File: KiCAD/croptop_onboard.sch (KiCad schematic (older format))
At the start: 64 parts, among them SW1 BTNA, SW2 BTNB, SW3 BTNC, SW4 BTND, U12 Si7006-A20, U13 UCAM-M8Q, U14 W25N01GV, U15 LIS3DH

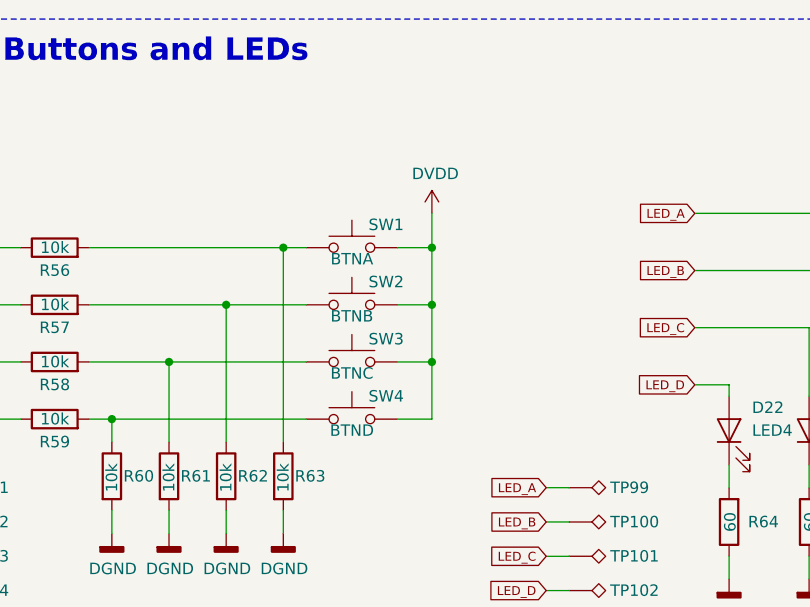
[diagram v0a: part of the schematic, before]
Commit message: Got to PCB layout
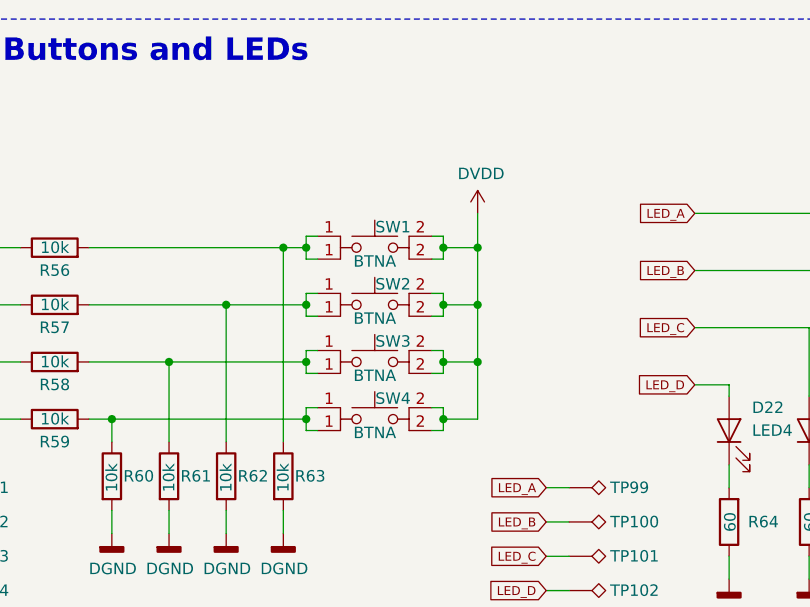
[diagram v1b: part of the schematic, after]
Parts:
- removed SW1: BTNA, symbol Switch:SW_Push
- removed SW2: BTNB, symbol Switch:SW_Push
- removed SW3: BTNC, symbol Switch:SW_Push
- removed SW4: BTND, symbol Switch:SW_Push
- added SW1, SW2, SW3, SW4: BTNA, Button_Switch_SMD:SW_SPST_PTS645, symbol CropTop:SW_Push
- U12: footprint (none) -> croptop:SI7006
- U13: footprint (none) -> croptop:GPS
- U14: footprint (none) -> croptop:W25N01GV
- U15: footprint (none) -> Package_LGA:LGA-16_3x3mm_P0.5mm_LayoutBorder3x5y
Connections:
- net DVDD: now also SW1.2, SW2.2, SW3.2, SW4.2
- net at R59.2, R60.1: now also SW4.1
- net at R58.2, R61.1: now also SW3.1
- net at R57.2, R62.1: now also SW2.1
- net at R56.2, R63.1: now also SW1.1
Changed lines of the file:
@@
 F 0 "U13" H 2500 3125 50  0000 C CNN
 F 1 "UCAM-M8Q" H 2500 3034 50  0000 C CNN
-F 2 "" H 2450 3000 50  0001 C CNN
+F 2 "croptop:GPS" H 2450 3000 50  0001 C CNN
 F 3 "" H 2450 3000 50  0001 C CNN
 	1    2500 2150
@@
 F 0 "U15" H 6900 2950 50  0000 C CNN
 F 1 "LIS3DH" H 7450 2950 50  0000 C CNN
-F 2 "" H 7100 2050 50  0001 C CNN
+F 2 "Package_LGA:LGA-16_3x3mm_P0.5mm_LayoutBorder3x5y" H 7100 2050 50  0001 C CNN
 F 3 "" H 7100 2050 50  0001 C CNN
 	1    7200 2350
@@
 F 0 "U12" H 2050 7275 50  0000 C CNN
 F 1 "Si7006-A20" H 2050 7184 50  0000 C CNN
-F 2 "" H 2050 6950 50  0001 C CNN
+F 2 "croptop:SI7006" H 2050 6950 50  0001 C CNN
 F 3 "" H 2050 6950 50  0001 C CNN
 	1    2050 6950
@@
 F 0 "U14" H 2600 5217 50  0000 C CNN
 F 1 "W25N01GV" H 2600 5126 50  0000 C CNN
-F 2 "" H 2450 4600 50  0001 C CNN
+F 2 "croptop:W25N01GV" H 2450 4600 50  0001 C CNN
 F 3 "" H 2450 4600 50  0001 C CNN
 	1    2600 4800
@@
 	0    -1   -1   0
 $EndComp
-$Comp
-L Switch:SW_Push SW?
-U 1 1 5CA26BD2
-P 7200 4900
-AR Path="/5CA26BD2" Ref="SW?"  Part="1"
-AR Path="/66A201BE/5CA26BD2" Ref="SW?"  Part="1"
-AR Path="/66A12230/5CA26BD2" Ref="SW1"  Part="1"
-F 0 "SW1" H 7350 5000 50  0000 C CNN
-F 1 "BTNA" H 7200 4850 50  0000 C CNN
-F 2 "" H 7200 5100 50  0001 C CNN
-F 3 "" H 7200 5100 50  0001 C CNN
-	1    7200 4900
-	1    0    0    -1
-$EndComp
-$Comp
-L Switch:SW_Push SW?
-U 1 1 5CA26BD9
-P 7200 5150
-AR Path="/5CA26BD9" Ref="SW?"  Part="1"
-AR Path="/66A201BE/5CA26BD9" Ref="SW?"  Part="1"
-AR Path="/66A12230/5CA26BD9" Ref="SW2"  Part="1"
-F 0 "SW2" H 7350 5250 50  0000 C CNN
-F 1 "BTNB" H 7200 5100 50  0000 C CNN
-F 2 "" H 7200 5350 50  0001 C CNN
-F 3 "" H 7200 5350 50  0001 C CNN
-	1    7200 5150
-	1    0    0    -1
-$EndComp
-$Comp
-L Switch:SW_Push SW?
-U 1 1 5CA26BE0
-P 7200 5400
-AR Path="/5CA26BE0" Ref="SW?"  Part="1"
-AR Path="/66A201BE/5CA26BE0" Ref="SW?"  Part="1"
-AR Path="/66A12230/5CA26BE0" Ref="SW3"  Part="1"
-F 0 "SW3" H 7350 5500 50  0000 C CNN
-F 1 "BTNC" H 7200 5350 50  0000 C CNN
-F 2 "" H 7200 5600 50  0001 C CNN
-F 3 "" H 7200 5600 50  0001 C CNN
-	1    7200 5400
-	1    0    0    -1
-$EndComp
-$Comp
-L Switch:SW_Push SW?
-U 1 1 5CA26BE7
-P 7200 5650
-AR Path="/5CA26BE7" Ref="SW?"  Part="1"
-AR Path="/66A201BE/5CA26BE7" Ref="SW?"  Part="1"
-AR Path="/66A12230/5CA26BE7" Ref="SW4"  Part="1"
-F 0 "SW4" H 7350 5750 50  0000 C CNN
-F 1 "BTND" H 7200 5600 50  0000 C CNN
-F 2 "" H 7200 5850 50  0001 C CNN
-F 3 "" H 7200 5850 50  0001 C CNN
-	1    7200 5650
-	1    0    0    -1
-$EndComp
-Wire Wire Line
-	7550 4750 7550 4900
-Wire Wire Line
-	7550 5650 7400 5650
-Wire Wire Line
-	7550 5400 7400 5400
-Connection ~ 7550 5400
-Wire Wire Line
-	7550 5400 7550 5650
-Wire Wire Line
-	7400 5150 7550 5150
-Connection ~ 7550 5150
-Wire Wire Line
-	7550 5150 7550 5400
-Wire Wire Line
-	7400 4900 7550 4900
-Connection ~ 7550 4900
-Wire Wire Line
-	7550 4900 7550 5150
+Wire Wire Line
+	7750 4750 7750 4900
+Wire Wire Line
+	7750 5650 7600 5650
+Wire Wire Line
+	7750 5400 7600 5400
+Connection ~ 7750 5400
+Wire Wire Line
+	7750 5400 7750 5650
+Wire Wire Line
+	7600 5150 7750 5150
+Connection ~ 7750 5150
+Wire Wire Line
+	7750 5150 7750 5400
+Wire Wire Line
+	7600 4900 7750 4900
+Connection ~ 7750 4900
+Wire Wire Line
+	7750 4900 7750 5150
 Wire Wire Line
 	7000 5650 6150 5650
@@
 L CropTop:DVDD #PWR0174
 U 1 1 5CA26C95
-P 7550 4750
-F 0 "#PWR0174" H 7550 4600 50  0001 C CNN
-F 1 "DVDD" H 7565 4923 50  0000 C CNN
-F 2 "" H 7550 4750 50  0001 C CNN
-F 3 "" H 7550 4750 50  0001 C CNN
-	1    7550 4750
+P 7750 4750
+F 0 "#PWR0174" H 7750 4600 50  0001 C CNN
+F 1 "DVDD" H 7765 4923 50  0000 C CNN
+F 2 "" H 7750 4750 50  0001 C CNN
+F 3 "" H 7750 4750 50  0001 C CNN
+	1    7750 4750
 	1    0    0    -1
 $EndComp
@@
 	0    1    1    0
 $EndComp
+$Comp
+L CropTop:SW_Push SW1
+U 1 1 5DF6569F
+P 7300 4750
+F 0 "SW1" H 7380 4690 50  0000 C CNN
+F 1 "BTNA" H 7300 4540 50  0000 C CNN
+F 2 "Button_Switch_SMD:SW_SPST_PTS645" H 7300 4950 50  0001 C CNN
+F 3 "" H 7300 4950 50  0001 C CNN
+	1    7300 4750
+	1    0    0    -1
+$EndComp
+$Comp
+L CropTop:SW_Push SW2
+U 1 1 5DF7A64A
+P 7300 5000
+F 0 "SW2" H 7380 4940 50  0000 C CNN
+F 1 "BTNA" H 7300 4790 50  0000 C CNN
+F 2 "Button_Switch_SMD:SW_SPST_PTS645" H 7300 5200 50  0001 C CNN
+F 3 "" H 7300 5200 50  0001 C CNN
+	1    7300 5000
+	1    0    0    -1
+$EndComp
+$Comp
+L CropTop:SW_Push SW3
+U 1 1 5DF8489F
+P 7300 5250
+F 0 "SW3" H 7380 5190 50  0000 C CNN
+F 1 "BTNA" H 7300 5040 50  0000 C CNN
+F 2 "Button_Switch_SMD:SW_SPST_PTS645" H 7300 5450 50  0001 C CNN
+F 3 "" H 7300 5450 50  0001 C CNN
+	1    7300 5250
+	1    0    0    -1
+$EndComp
+$Comp
+L CropTop:SW_Push SW4
+U 1 1 5DF8EB38
+P 7300 5500
+F 0 "SW4" H 7380 5440 50  0000 C CNN
+F 1 "BTNA" H 7300 5290 50  0000 C CNN
+F 2 "Button_Switch_SMD:SW_SPST_PTS645" H 7300 5700 50  0001 C CNN
+F 3 "" H 7300 5700 50  0001 C CNN
+	1    7300 5500
+	1    0    0    -1
+$EndComp
+Wire Wire Line
+	7000 4900 7000 4850
+Wire Wire Line
+	7000 4850 7050 4850
+Wire Wire Line
+	7000 4900 7000 4950
+Wire Wire Line
+	7000 4950 7050 4950
+Connection ~ 7000 4900
+Wire Wire Line
+	7000 5150 7000 5100
+Wire Wire Line
+	7000 5100 7050 5100
+Wire Wire Line
+	7000 5150 7000 5200
+Wire Wire Line
+	7000 5200 7050 5200
+Connection ~ 7000 5150
+Wire Wire Line
+	7000 5400 7000 5350
+Wire Wire Line
+	7000 5350 7050 5350
+Wire Wire Line
+	7000 5400 7000 5450
+Wire Wire Line
+	7000 5450 7050 5450
+Connection ~ 7000 5400
+Wire Wire Line
+	7000 5650 7000 5600
+Wire Wire Line
+	7000 5600 7050 5600
+Wire Wire Line
+	7000 5650 7000 5700
+Wire Wire Line
+	7000 5700 7050 5700
+Connection ~ 7000 5650
+Wire Wire Line
+	7550 5700 7600 5700
+Wire Wire Line
+	7600 5700 7600 5650
+Wire Wire Line
+	7550 5600 7600 5600
+Wire Wire Line
+	7600 5600 7600 5650
+Connection ~ 7600 5650
+Wire Wire Line
+	7550 5450 7600 5450
+Wire Wire Line
+	7600 5450 7600 5400
+Wire Wire Line
+	7600 5400 7600 5350
+Wire Wire Line
+	7600 5350 7550 5350
+Connection ~ 7600 5400
+Wire Wire Line
+	7550 5200 7600 5200
+Wire Wire Line
+	7600 5200 7600 5150
+Wire Wire Line
+	7600 5100 7550 5100
+Wire Wire Line
+	7600 5150 7600 5100
+Connection ~ 7600 5150
+Wire Wire Line
+	7550 4950 7600 4950
+Wire Wire Line
+	7600 4950 7600 4900
+Wire Wire Line
+	7600 4850 7550 4850
+Wire Wire Line
+	7600 4850 7600 4900
+Connection ~ 7600 4900
 $EndSCHEMATC

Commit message: Dec 18th
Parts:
- removed R58, R59, R60, R61: 10k, Resistor_SMD:R_0402_1005Metric, symbol Device:R
- removed SW3, SW4: BTNA, Button_Switch_SMD:SW_SPST_PTS645, symbol CropTop:SW_Push
- removed TP93, TP94: TestPoint_Alt, TestPoint:TestPoint_Pad_D2.0mm, symbol Connector:TestPoint_Alt
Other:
- moved on the sheet: R62, R63, TP95

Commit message: Finished working board
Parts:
- removed C64, C66, C67, C70: 10uF, Capacitor_SMD:C_0805_2012Metric, symbol Device:C
- removed D22: LED4, LED_SMD:LED_0805_2012Metric, symbol Device:LED
- removed D23: LED3, LED_SMD:LED_0805_2012Metric, symbol Device:LED
- removed R64, R65: 60, Resistor_SMD:R_0402_1005Metric, symbol Device:R
- removed TP101, TP102, TP103, TP81, TP84, TP87, TP95, TP98: TestPoint_Alt, TestPoint:TestPoint_Pad_D2.0mm, symbol Connector:TestPoint_Alt
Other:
- moved on the sheet: C65, C68, C69, C71, D24, D25, R66, R67, TP100, TP99

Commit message: Changed testpoint size
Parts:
- TP100, TP76, TP77, TP78, TP79, TP80, TP82, TP83, TP85, TP86, TP88, TP89, TP90, TP91, TP92, TP96, TP97, TP99: footprint TestPoint:TestPoint_Pad_D2.0mm -> TestPoint:TestPoint_Pad_1.0x1.0mm
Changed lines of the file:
@@
 F 0 "TP99" V 5350 5780 50  0000 L CNN
 F 1 "TestPoint_Alt" V 5385 5785 50  0001 L CNN
-F 2 "TestPoint:TestPoint_Pad_D2.0mm" H 5550 5600 50  0001 C CNN
+F 2 "TestPoint:TestPoint_Pad_1.0x1.0mm" H 5550 5600 50  0001 C CNN
 F 3 "~" H 5550 5600 50  0001 C CNN
 	1    5350 5600
@@
 F 0 "TP100" V 5350 5930 50  0000 L CNN
 F 1 "TestPoint_Alt" V 5385 5935 50  0001 L CNN
-F 2 "TestPoint:TestPoint_Pad_D2.0mm" H 5550 5750 50  0001 C CNN
+F 2 "TestPoint:TestPoint_Pad_1.0x1.0mm" H 5550 5750 50  0001 C CNN
 F 3 "~" H 5550 5750 50  0001 C CNN
 	1    5350 5750
@@
 F 0 "TP91" V 5350 6130 50  0000 L CNN
 F 1 "TestPoint_Alt" V 5385 6135 50  0001 L CNN
-F 2 "TestPoint:TestPoint_Pad_D2.0mm" H 5550 5950 50  0001 C CNN
+F 2 "TestPoint:TestPoint_Pad_1.0x1.0mm" H 5550 5950 50  0001 C CNN
 F 3 "~" H 5550 5950 50  0001 C CNN
 	1    5350 5950
@@
 F 0 "TP92" V 5350 6280 50  0000 L CNN
 F 1 "TestPoint_Alt" V 5385 6285 50  0001 L CNN
-F 2 "TestPoint:TestPoint_Pad_D2.0mm" H 5550 6100 50  0001 C CNN
+F 2 "TestPoint:TestPoint_Pad_1.0x1.0mm" H 5550 6100 50  0001 C CNN
 F 3 "~" H 5550 6100 50  0001 C CNN
 	1    5350 6100
@@
 F 0 "TP96" V 6150 3080 50  0000 L CNN
 F 1 "TestPoint_Alt" V 6185 3085 50  0001 L CNN
-F 2 "TestPoint:TestPoint_Pad_D2.0mm" H 6350 2900 50  0001 C CNN
+F 2 "TestPoint:TestPoint_Pad_1.0x1.0mm" H 6350 2900 50  0001 C CNN
 F 3 "~" H 6350 2900 50  0001 C CNN
 	1    6150 2900
@@
 F 0 "TP97" V 6150 3230 50  0000 L CNN
 F 1 "TestPoint_Alt" V 6185 3235 50  0001 L CNN
-F 2 "TestPoint:TestPoint_Pad_D2.0mm" H 6350 3050 50  0001 C CNN
+F 2 "TestPoint:TestPoint_Pad_1.0x1.0mm" H 6350 3050 50  0001 C CNN
 F 3 "~" H 6350 3050 50  0001 C CNN
 	1    6150 3050
@@
 F 0 "TP82" V 1700 7430 50  0000 L CNN
 F 1 "TestPoint_Alt" V 1735 7435 50  0001 L CNN
-F 2 "TestPoint:TestPoint_Pad_D2.0mm" H 1900 7250 50  0001 C CNN
+F 2 "TestPoint:TestPoint_Pad_1.0x1.0mm" H 1900 7250 50  0001 C CNN
 F 3 "~" H 1900 7250 50  0001 C CNN
 	1    1700 7250
@@
 F 0 "TP83" V 1700 7580 50  0000 L CNN
 F 1 "TestPoint_Alt" V 1735 7585 50  0001 L CNN
-F 2 "TestPoint:TestPoint_Pad_D2.0mm" H 1900 7400 50  0001 C CNN
+F 2 "TestPoint:TestPoint_Pad_1.0x1.0mm" H 1900 7400 50  0001 C CNN
 F 3 "~" H 1900 7400 50  0001 C CNN
 	1    1700 7400
@@
 F 0 "TP79" V 1550 3330 50  0000 L CNN
 F 1 "TestPoint_Alt" V 1585 3335 50  0001 L CNN
-F 2 "TestPoint:TestPoint_Pad_D2.0mm" H 1750 3150 50  0001 C CNN
+F 2 "TestPoint:TestPoint_Pad_1.0x1.0mm" H 1750 3150 50  0001 C CNN
 F 3 "~" H 1750 3150 50  0001 C CNN
 	1    1550 3150
@@
 F 0 "TP80" V 1550 3480 50  0000 L CNN
 F 1 "TestPoint_Alt" V 1585 3485 50  0001 L CNN
-F 2 "TestPoint:TestPoint_Pad_D2.0mm" H 1750 3300 50  0001 C CNN
+F 2 "TestPoint:TestPoint_Pad_1.0x1.0mm" H 1750 3300 50  0001 C CNN
 F 3 "~" H 1750 3300 50  0001 C CNN
 	1    1550 3300
@@
 F 0 "TP89" V 2350 3480 50  0000 L CNN
 F 1 "TestPoint_Alt" V 2385 3485 50  0001 L CNN
-F 2 "TestPoint:TestPoint_Pad_D2.0mm" H 2550 3300 50  0001 C CNN
+F 2 "TestPoint:TestPoint_Pad_1.0x1.0mm" H 2550 3300 50  0001 C CNN
 F 3 "~" H 2550 3300 50  0001 C CNN
 	1    2350 3300
@@
 F 0 "TP90" V 2350 3630 50  0000 L CNN
 F 1 "TestPoint_Alt" V 2385 3635 50  0001 L CNN
-F 2 "TestPoint:TestPoint_Pad_D2.0mm" H 2550 3450 50  0001 C CNN
+F 2 "TestPoint:TestPoint_Pad_1.0x1.0mm" H 2550 3450 50  0001 C CNN
 F 3 "~" H 2550 3450 50  0001 C CNN
 	1    2350 3450
@@
 F 0 "TP88" V 2350 3330 50  0000 L CNN
 F 1 "TestPoint_Alt" V 2385 3335 50  0001 L CNN
-F 2 "TestPoint:TestPoint_Pad_D2.0mm" H 2550 3150 50  0001 C CNN
+F 2 "TestPoint:TestPoint_Pad_1.0x1.0mm" H 2550 3150 50  0001 C CNN
 F 3 "~" H 2550 3150 50  0001 C CNN
 	1    2350 3150
@@
 F 0 "TP76" V 1050 5380 50  0000 L CNN
 F 1 "TestPoint_Alt" V 1085 5385 50  0001 L CNN
-F 2 "TestPoint:TestPoint_Pad_D2.0mm" H 1250 5200 50  0001 C CNN
+F 2 "TestPoint:TestPoint_Pad_1.0x1.0mm" H 1250 5200 50  0001 C CNN
 F 3 "~" H 1250 5200 50  0001 C CNN
 	1    1050 5200
@@
 F 0 "TP77" V 1050 5530 50  0000 L CNN
 F 1 "TestPoint_Alt" V 1085 5535 50  0001 L CNN
-F 2 "TestPoint:TestPoint_Pad_D2.0mm" H 1250 5350 50  0001 C CNN
+F 2 "TestPoint:TestPoint_Pad_1.0x1.0mm" H 1250 5350 50  0001 C CNN
 F 3 "~" H 1250 5350 50  0001 C CNN
 	1    1050 5350
@@
 F 0 "TP78" V 1050 5680 50  0000 L CNN
 F 1 "TestPoint_Alt" V 1085 5685 50  0001 L CNN
-F 2 "TestPoint:TestPoint_Pad_D2.0mm" H 1250 5500 50  0001 C CNN
+F 2 "TestPoint:TestPoint_Pad_1.0x1.0mm" H 1250 5500 50  0001 C CNN
 F 3 "~" H 1250 5500 50  0001 C CNN
 	1    1050 5500
@@
 F 0 "TP85" V 1950 5380 50  0000 L CNN
 F 1 "TestPoint_Alt" V 1985 5385 50  0001 L CNN
-F 2 "TestPoint:TestPoint_Pad_D2.0mm" H 2150 5200 50  0001 C CNN
+F 2 "TestPoint:TestPoint_Pad_1.0x1.0mm" H 2150 5200 50  0001 C CNN
 F 3 "~" H 2150 5200 50  0001 C CNN
 	1    1950 5200
@@
 F 0 "TP86" V 1950 5530 50  0000 L CNN
 F 1 "TestPoint_Alt" V 1985 5535 50  0001 L CNN
-F 2 "TestPoint:TestPoint_Pad_D2.0mm" H 2150 5350 50  0001 C CNN
+F 2 "TestPoint:TestPoint_Pad_1.0x1.0mm" H 2150 5350 50  0001 C CNN
 F 3 "~" H 2150 5350 50  0001 C CNN
 	1    1950 5350

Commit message: Complete PCB version 1
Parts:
- removed TP76, TP77, TP79, TP80, TP96, TP97: TestPoint_Alt, TestPoint:TestPoint_Pad_1.0x1.0mm, symbol Connector:TestPoint_Alt
- TP100, TP78, TP82, TP83, TP85, TP86, TP88, TP89, TP90, TP91, TP92, TP99: footprint TestPoint:TestPoint_Pad_1.0x1.0mm -> croptop:TestPoint
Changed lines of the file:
@@
 F 0 "TP99" V 5350 5780 50  0000 L CNN
 F 1 "TestPoint_Alt" V 5385 5785 50  0001 L CNN
-F 2 "TestPoint:TestPoint_Pad_1.0x1.0mm" H 5550 5600 50  0001 C CNN
+F 2 "croptop:TestPoint" H 5550 5600 50  0001 C CNN
 F 3 "~" H 5550 5600 50  0001 C CNN
 	1    5350 5600
@@
 F 0 "TP100" V 5350 5930 50  0000 L CNN
 F 1 "TestPoint_Alt" V 5385 5935 50  0001 L CNN
-F 2 "TestPoint:TestPoint_Pad_1.0x1.0mm" H 5550 5750 50  0001 C CNN
+F 2 "croptop:TestPoint" H 5550 5750 50  0001 C CNN
 F 3 "~" H 5550 5750 50  0001 C CNN
 	1    5350 5750
@@
 F 0 "TP91" V 5350 6130 50  0000 L CNN
 F 1 "TestPoint_Alt" V 5385 6135 50  0001 L CNN
-F 2 "TestPoint:TestPoint_Pad_1.0x1.0mm" H 5550 5950 50  0001 C CNN
+F 2 "croptop:TestPoint" H 5550 5950 50  0001 C CNN
 F 3 "~" H 5550 5950 50  0001 C CNN
 	1    5350 5950
@@
 F 0 "TP92" V 5350 6280 50  0000 L CNN
 F 1 "TestPoint_Alt" V 5385 6285 50  0001 L CNN
-F 2 "TestPoint:TestPoint_Pad_1.0x1.0mm" H 5550 6100 50  0001 C CNN
+F 2 "croptop:TestPoint" H 5550 6100 50  0001 C CNN
 F 3 "~" H 5550 6100 50  0001 C CNN
 	1    5350 6100
 	0    1    1    0
 $EndComp
-$Comp
-L Connector:TestPoint_Alt TP?
-U 1 1 5C32FA6C
-P 6150 2900
-AR Path="/64809F0C/5C32FA6C" Ref="TP?"  Part="1"
-AR Path="/66A12230/5C32FA6C" Ref="TP96"  Part="1"
-F 0 "TP96" V 6150 3080 50  0000 L CNN
-F 1 "TestPoint_Alt" V 6185 3085 50  0001 L CNN
-F 2 "TestPoint:TestPoint_Pad_1.0x1.0mm" H 6350 2900 50  0001 C CNN
-F 3 "~" H 6350 2900 50  0001 C CNN
-	1    6150 2900
-	0    1    1    0
-$EndComp
-$Comp
-L Connector:TestPoint_Alt TP?
-U 1 1 5C32FA73
-P 6150 3050
-AR Path="/64809F0C/5C32FA73" Ref="TP?"  Part="1"
-AR Path="/66A12230/5C32FA73" Ref="TP97"  Part="1"
-F 0 "TP97" V 6150 3230 50  0000 L CNN
-F 1 "TestPoint_Alt" V 6185 3235 50  0001 L CNN
-F 2 "TestPoint:TestPoint_Pad_1.0x1.0mm" H 6350 3050 50  0001 C CNN
-F 3 "~" H 6350 3050 50  0001 C CNN
-	1    6150 3050
-	0    1    1    0
-$EndComp
-Wire Wire Line
-	6150 2900 6050 2900
-Wire Wire Line
-	6050 3050 6150 3050
-Text GLabel 6050 2900 0    39   Input ~ 0
-SDA
-Text GLabel 6050 3050 0    39   Input ~ 0
-SCL
 $Comp
 L Connector:TestPoint_Alt TP?
@@
 F 0 "TP82" V 1700 7430 50  0000 L CNN
 F 1 "TestPoint_Alt" V 1735 7435 50  0001 L CNN
-F 2 "TestPoint:TestPoint_Pad_1.0x1.0mm" H 1900 7250 50  0001 C CNN
+F 2 "croptop:TestPoint" H 1900 7250 50  0001 C CNN
 F 3 "~" H 1900 7250 50  0001 C CNN
 	1    1700 7250
@@
 F 0 "TP83" V 1700 7580 50  0000 L CNN
 F 1 "TestPoint_Alt" V 1735 7585 50  0001 L CNN
-F 2 "TestPoint:TestPoint_Pad_1.0x1.0mm" H 1900 7400 50  0001 C CNN
+F 2 "croptop:TestPoint" H 1900 7400 50  0001 C CNN
 F 3 "~" H 1900 7400 50  0001 C CNN
 	1    1700 7400
@@
 SDA
 Text GLabel 1600 7400 0    39   Input ~ 0
-SCL
-$Comp
-L Connector:TestPoint_Alt TP?
-U 1 1 5C3834AD
-P 1550 3150
-AR Path="/64809F0C/5C3834AD" Ref="TP?"  Part="1"
-AR Path="/66A12230/5C3834AD" Ref="TP79"  Part="1"
-F 0 "TP79" V 1550 3330 50  0000 L CNN
-F 1 "TestPoint_Alt" V 1585 3335 50  0001 L CNN
-F 2 "TestPoint:TestPoint_Pad_1.0x1.0mm" H 1750 3150 50  0001 C CNN
-F 3 "~" H 1750 3150 50  0001 C CNN
-	1    1550 3150
-	0    1    1    0
-$EndComp
-$Comp
-L Connector:TestPoint_Alt TP?
-U 1 1 5C3834B4
-P 1550 3300
-AR Path="/64809F0C/5C3834B4" Ref="TP?"  Part="1"
-AR Path="/66A12230/5C3834B4" Ref="TP80"  Part="1"
-F 0 "TP80" V 1550 3480 50  0000 L CNN
-F 1 "TestPoint_Alt" V 1585 3485 50  0001 L CNN
-F 2 "TestPoint:TestPoint_Pad_1.0x1.0mm" H 1750 3300 50  0001 C CNN
-F 3 "~" H 1750 3300 50  0001 C CNN
-	1    1550 3300
-	0    1    1    0
-$EndComp
-Wire Wire Line
-	1550 3150 1450 3150
-Wire Wire Line
-	1450 3300 1550 3300
-Text GLabel 1450 3150 0    39   Input ~ 0
-SDA
-Text GLabel 1450 3300 0    39   Input ~ 0
 SCL
 Text GLabel 2250 3300 0    39   Input ~ 0
@@
 F 0 "TP89" V 2350 3480 50  0000 L CNN
 F 1 "TestPoint_Alt" V 2385 3485 50  0001 L CNN
-F 2 "TestPoint:TestPoint_Pad_1.0x1.0mm" H 2550 3300 50  0001 C CNN
+F 2 "croptop:TestPoint" H 2550 3300 50  0001 C CNN
 F 3 "~" H 2550 3300 50  0001 C CNN
 	1    2350 3300
@@
 F 0 "TP90" V 2350 3630 50  0000 L CNN
 F 1 "TestPoint_Alt" V 2385 3635 50  0001 L CNN
-F 2 "TestPoint:TestPoint_Pad_1.0x1.0mm" H 2550 3450 50  0001 C CNN
+F 2 "croptop:TestPoint" H 2550 3450 50  0001 C CNN
 F 3 "~" H 2550 3450 50  0001 C CNN
 	1    2350 3450
@@
 F 0 "TP88" V 2350 3330 50  0000 L CNN
 F 1 "TestPoint_Alt" V 2385 3335 50  0001 L CNN
-F 2 "TestPoint:TestPoint_Pad_1.0x1.0mm" H 2550 3150 50  0001 C CNN
+F 2 "croptop:TestPoint" H 2550 3150 50  0001 C CNN
 F 3 "~" H 2550 3150 50  0001 C CNN
 	1    2350 3150
@@
 Wire Wire Line
 	2350 3150 2250 3150
-Text GLabel 950  5200 0    39   Input ~ 0
-SCLK
-Text GLabel 950  5350 0    39   Input ~ 0
-MOSI
 Text GLabel 950  5500 0    39   Input ~ 0
 NAND_CS
 Wire Wire Line
-	1050 5200 950  5200
-Wire Wire Line
-	950  5350 1050 5350
-Wire Wire Line
 	1050 5500 950  5500
-$Comp
-L Connector:TestPoint_Alt TP?
-U 1 1 5C45BD90
-P 1050 5200
-AR Path="/64809F0C/5C45BD90" Ref="TP?"  Part="1"
-AR Path="/66A12230/5C45BD90" Ref="TP76"  Part="1"
-F 0 "TP76" V 1050 5380 50  0000 L CNN
-F 1 "TestPoint_Alt" V 1085 5385 50  0001 L CNN
-F 2 "TestPoint:TestPoint_Pad_1.0x1.0mm" H 1250 5200 50  0001 C CNN
-F 3 "~" H 1250 5200 50  0001 C CNN
-	1    1050 5200
-	0    1    1    0
-$EndComp
-$Comp
-L Connector:TestPoint_Alt TP?
-U 1 1 5C45BD97
-P 1050 5350
-AR Path="/64809F0C/5C45BD97" Ref="TP?"  Part="1"
-AR Path="/66A12230/5C45BD97" Ref="TP77"  Part="1"
-F 0 "TP77" V 1050 5530 50  0000 L CNN
-F 1 "TestPoint_Alt" V 1085 5535 50  0001 L CNN
-F 2 "TestPoint:TestPoint_Pad_1.0x1.0mm" H 1250 5350 50  0001 C CNN
-F 3 "~" H 1250 5350 50  0001 C CNN
-	1    1050 5350
-	0    1    1    0
-$EndComp
 $Comp
 L Connector:TestPoint_Alt TP?
@@
 F 0 "TP78" V 1050 5680 50  0000 L CNN
 F 1 "TestPoint_Alt" V 1085 5685 50  0001 L CNN
-F 2 "TestPoint:TestPoint_Pad_1.0x1.0mm" H 1250 5500 50  0001 C CNN
+F 2 "croptop:TestPoint" H 1250 5500 50  0001 C CNN
 F 3 "~" H 1250 5500 50  0001 C CNN
 	1    1050 5500
@@
 F 0 "TP85" V 1950 5380 50  0000 L CNN
 F 1 "TestPoint_Alt" V 1985 5385 50  0001 L CNN
-F 2 "TestPoint:TestPoint_Pad_1.0x1.0mm" H 2150 5200 50  0001 C CNN
+F 2 "croptop:TestPoint" H 2150 5200 50  0001 C CNN
 F 3 "~" H 2150 5200 50  0001 C CNN
 	1    1950 5200
@@
 F 0 "TP86" V 1950 5530 50  0000 L CNN
 F 1 "TestPoint_Alt" V 1985 5535 50  0001 L CNN
-F 2 "TestPoint:TestPoint_Pad_1.0x1.0mm" H 2150 5350 50  0001 C CNN
+F 2 "croptop:TestPoint" H 2150 5350 50  0001 C CNN
 F 3 "~" H 2150 5350 50  0001 C CNN
 	1    1950 5350
